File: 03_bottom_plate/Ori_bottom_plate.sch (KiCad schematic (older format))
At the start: 72 parts, among them U1 HOLE, U10 HOLE, U11 HOLE, U12 HOLE, U13 HOLE, U14 HOLE, U15 HOLE, U16 HOLE, U17 HOLE, U18 HOLE, U19 HOLE, U2 HOLE, U20 HOLE, U21 HOLE, U22 HOLE, U23 HOLE, U24 HOLE, U25 HOLE, U26 HOLE, U27 HOLE, U28 HOLE, U29 HOLE, U3 HOLE, U30 HOLE, U31 HOLE, U32 HOLE, U33 HOLE, U34 HOLE, U35 HOLE, U36 HOLE, U37 HOLE, U38 HOLE, U39 HOLE, U4 HOLE, U40 HOLE, U41 HOLE, U42 HOLE, U43 HOLE, U44 HOLE, U45 HOLE, U46 HOLE, U47 HOLE, U48 HOLE, U49 HOLE, U5 HOLE, U53 HOLE, U57 HOLE, U6 HOLE, U61 HOLE, U7 HOLE, U8 HOLE, U9 HOLE

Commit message: 19.05mm spacing; move macro column to right side
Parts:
- removed H1, H2, H3, H4, H5, H6: MountingHole, random-keyboard-parts:Generic-Mounthole, symbol Mechanical:MountingHole
- added D1: DIODE, Keeb_footprints:D_SOD-123_modified, symbol component:DIODE
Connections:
- new net GND: D1.2 (K)
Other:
- moved on the sheet: U49, U53, U57, U61
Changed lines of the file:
@@
 EESchema Schematic File Version 4
-LIBS:Ori_bottom_plate-cache
+LIBS:ori_bottom_plate-cache
 EELAYER 30 0
 EELAYER END
@@
 Comment4 ""
 $EndDescr
-$Comp
-L Mechanical:MountingHole H2
-U 1 1 5DAFB0AC
-P 2600 3300
-F 0 "H2" H 2700 3346 50  0000 L CNN
-F 1 "MountingHole" H 2700 3255 50  0000 L CNN
-F 2 "random-keyboard-parts:Generic-Mounthole" H 2600 3300 50  0001 C CNN
-F 3 "~" H 2600 3300 50  0001 C CNN
-	1    2600 3300
-	1    0    0    -1
-$EndComp
-$Comp
-L Mechanical:MountingHole H1
-U 1 1 5DAFBA19
-P 2600 3100
-F 0 "H1" H 2700 3146 50  0000 L CNN
-F 1 "MountingHole" H 2700 3055 50  0000 L CNN
-F 2 "random-keyboard-parts:Generic-Mounthole" H 2600 3100 50  0001 C CNN
-F 3 "~" H 2600 3100 50  0001 C CNN
-	1    2600 3100
-	1    0    0    -1
-$EndComp
-$Comp
-L Mechanical:MountingHole H3
-U 1 1 5DAFC41A
-P 2600 3500
-F 0 "H3" H 2700 3546 50  0000 L CNN
-F 1 "MountingHole" H 2700 3455 50  0000 L CNN
-F 2 "random-keyboard-parts:Generic-Mounthole" H 2600 3500 50  0001 C CNN
-F 3 "~" H 2600 3500 50  0001 C CNN
-	1    2600 3500
-	1    0    0    -1
-$EndComp
-$Comp
-L Mechanical:MountingHole H4
-U 1 1 5DAFCFC0
-P 2600 3700
-F 0 "H4" H 2700 3746 50  0000 L CNN
-F 1 "MountingHole" H 2700 3655 50  0000 L CNN
-F 2 "random-keyboard-parts:Generic-Mounthole" H 2600 3700 50  0001 C CNN
-F 3 "~" H 2600 3700 50  0001 C CNN
-	1    2600 3700
-	1    0    0    -1
-$EndComp
-$Comp
-L Mechanical:MountingHole H5
-U 1 1 5DAFD908
-P 2600 3900
-F 0 "H5" H 2700 3946 50  0000 L CNN
-F 1 "MountingHole" H 2700 3855 50  0000 L CNN
-F 2 "random-keyboard-parts:Generic-Mounthole" H 2600 3900 50  0001 C CNN
-F 3 "~" H 2600 3900 50  0001 C CNN
-	1    2600 3900
-	1    0    0    -1
-$EndComp
-$Comp
-L Mechanical:MountingHole H6
-U 1 1 5DAFE1B7
-P 2600 4100
-F 0 "H6" H 2700 4146 50  0000 L CNN
-F 1 "MountingHole" H 2700 4055 50  0000 L CNN
-F 2 "random-keyboard-parts:Generic-Mounthole" H 2600 4100 50  0001 C CNN
-F 3 "~" H 2600 4100 50  0001 C CNN
-	1    2600 4100
-	1    0    0    -1
-$EndComp
 Text Notes 2850 4750 0    50   ~ 0
 Screw Holes
@@
 L lets_split-cache:HOLE U49
 U 1 1 5F4BC82B
-P 2250 1550
-F 0 "U49" H 2150 1600 60  0000 L CNN
-F 1 "HOLE" H 2150 1500 60  0000 L CNN
-F 2 "Keeb_footprints:MX100_outline" H 2250 1550 60  0001 C CNN
-F 3 "" H 2250 1550 60  0001 C CNN
-	1    2250 1550
+P 6350 1550
+F 0 "U49" H 6250 1600 60  0000 L CNN
+F 1 "HOLE" H 6250 1500 60  0000 L CNN
+F 2 "Keeb_footprints:MX100_outline" H 6350 1550 60  0001 C CNN
+F 3 "" H 6350 1550 60  0001 C CNN
+	1    6350 1550
 	1    0    0    -1
 $EndComp
@@
 L lets_split-cache:HOLE U53
 U 1 1 5F4BC843
-P 2250 1850
-F 0 "U53" H 2150 1900 60  0000 L CNN
-F 1 "HOLE" H 2150 1800 60  0000 L CNN
-F 2 "Keeb_footprints:MX100_outline" H 2250 1850 60  0001 C CNN
-F 3 "" H 2250 1850 60  0001 C CNN
-	1    2250 1850
+P 6350 1850
+F 0 "U53" H 6250 1900 60  0000 L CNN
+F 1 "HOLE" H 6250 1800 60  0000 L CNN
+F 2 "Keeb_footprints:MX100_outline" H 6350 1850 60  0001 C CNN
+F 3 "" H 6350 1850 60  0001 C CNN
+	1    6350 1850
 	1    0    0    -1
 $EndComp
@@
 L lets_split-cache:HOLE U57
 U 1 1 5F4BC85B
-P 2250 2150
-F 0 "U57" H 2150 2200 60  0000 L CNN
-F 1 "HOLE" H 2150 2100 60  0000 L CNN
-F 2 "Keeb_footprints:MX100_outline" H 2250 2150 60  0001 C CNN
-F 3 "" H 2250 2150 60  0001 C CNN
-	1    2250 2150
+P 6350 2150
+F 0 "U57" H 6250 2200 60  0000 L CNN
+F 1 "HOLE" H 6250 2100 60  0000 L CNN
+F 2 "Keeb_footprints:MX100_outline" H 6350 2150 60  0001 C CNN
+F 3 "" H 6350 2150 60  0001 C CNN
+	1    6350 2150
 	1    0    0    -1
 $EndComp
@@
 L lets_split-cache:HOLE U61
 U 1 1 5F4BC873
-P 2250 2450
-F 0 "U61" H 2150 2500 60  0000 L CNN
-F 1 "HOLE" H 2150 2400 60  0000 L CNN
-F 2 "Keeb_footprints:MX100_outline" H 2250 2450 60  0001 C CNN
-F 3 "" H 2250 2450 60  0001 C CNN
-	1    2250 2450
+P 6350 2450
+F 0 "U61" H 6250 2500 60  0000 L CNN
+F 1 "HOLE" H 6250 2400 60  0000 L CNN
+F 2 "Keeb_footprints:MX100_outline" H 6350 2450 60  0001 C CNN
+F 3 "" H 6350 2450 60  0001 C CNN
+	1    6350 2450
 	1    0    0    -1
 $EndComp
@@
 Wire Notes Line
 	5200 4350 4200 4350
+$Comp
+L component:DIODE D1
+U 1 1 60E9CF4B
+P 6350 3300
+F 0 "D1" H 6350 3492 40  0000 C CNN
+F 1 "DIODE" H 6350 3416 40  0000 C CNN
+F 2 "Keeb_footprints:D_SOD-123_modified" H 6350 3300 50  0001 C CNN
+F 3 "" H 6350 3300 50  0001 C CNN
+	1    6350 3300
+	1    0    0    -1
+$EndComp
+$Comp
+L power:GND #PWR0101
+U 1 1 60E9D8FE
+P 6550 3300
+F 0 "#PWR0101" H 6550 3050 50  0001 C CNN
+F 1 "GND" H 6555 3127 50  0000 C CNN
+F 2 "" H 6550 3300 50  0001 C CNN
+F 3 "" H 6550 3300 50  0001 C CNN
+	1    6550 3300
+	1    0    0    -1
+$EndComp
 $EndSCHEMATC

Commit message: Updated firmware
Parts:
- added H1, H2, H21, H22, H3, H4, H5, H6: MountingHole, random-keyboard-parts:Generic-Mounthole, symbol Mechanical:MountingHole
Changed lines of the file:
@@
 EESchema Schematic File Version 4
-LIBS:ori_bottom_plate-cache
 EELAYER 30 0
 EELAYER END
@@
 	1    0    0    -1
 $EndComp
+$Comp
+L Mechanical:MountingHole H1
+U 1 1 6111B67C
+P 2550 5000
+F 0 "H1" H 2650 5046 50  0000 L CNN
+F 1 "MountingHole" H 2650 4955 50  0000 L CNN
+F 2 "random-keyboard-parts:Generic-Mounthole" H 2550 5000 50  0001 C CNN
+F 3 "~" H 2550 5000 50  0001 C CNN
+	1    2550 5000
+	1    0    0    -1
+$EndComp
+$Comp
+L Mechanical:MountingHole H2
+U 1 1 6111B682
+P 2550 5200
+F 0 "H2" H 2650 5246 50  0000 L CNN
+F 1 "MountingHole" H 2650 5155 50  0000 L CNN
+F 2 "random-keyboard-parts:Generic-Mounthole" H 2550 5200 50  0001 C CNN
+F 3 "~" H 2550 5200 50  0001 C CNN
+	1    2550 5200
+	1    0    0    -1
+$EndComp
+$Comp
+L Mechanical:MountingHole H3
+U 1 1 6111B688
+P 2550 5400
+F 0 "H3" H 2650 5446 50  0000 L CNN
+F 1 "MountingHole" H 2650 5355 50  0000 L CNN
+F 2 "random-keyboard-parts:Generic-Mounthole" H 2550 5400 50  0001 C CNN
+F 3 "~" H 2550 5400 50  0001 C CNN
+	1    2550 5400
+	1    0    0    -1
+$EndComp
+$Comp
+L Mechanical:MountingHole H4
+U 1 1 6111B68E
+P 2550 5600
+F 0 "H4" H 2650 5646 50  0000 L CNN
+F 1 "MountingHole" H 2650 5555 50  0000 L CNN
+F 2 "random-keyboard-parts:Generic-Mounthole" H 2550 5600 50  0001 C CNN
+F 3 "~" H 2550 5600 50  0001 C CNN
+	1    2550 5600
+	1    0    0    -1
+$EndComp
+$Comp
+L Mechanical:MountingHole H5
+U 1 1 6111B694
+P 2550 5800
+F 0 "H5" H 2650 5846 50  0000 L CNN
+F 1 "MountingHole" H 2650 5755 50  0000 L CNN
+F 2 "random-keyboard-parts:Generic-Mounthole" H 2550 5800 50  0001 C CNN
+F 3 "~" H 2550 5800 50  0001 C CNN
+	1    2550 5800
+	1    0    0    -1
+$EndComp
+$Comp
+L Mechanical:MountingHole H6
+U 1 1 6111B69A
+P 2550 6000
+F 0 "H6" H 2650 6046 50  0000 L CNN
+F 1 "MountingHole" H 2650 5955 50  0000 L CNN
+F 2 "random-keyboard-parts:Generic-Mounthole" H 2550 6000 50  0001 C CNN
+F 3 "~" H 2550 6000 50  0001 C CNN
+	1    2550 6000
+	1    0    0    -1
+$EndComp
+$Comp
+L Mechanical:MountingHole H21
+U 1 1 6111ADF9
+P 3650 5050
+F 0 "H21" H 3750 5096 50  0000 L CNN
+F 1 "MountingHole" H 3750 5005 50  0000 L CNN
+F 2 "random-keyboard-parts:Generic-Mounthole" H 3650 5050 50  0001 C CNN
+F 3 "~" H 3650 5050 50  0001 C CNN
+	1    3650 5050
+	1    0    0    -1
+$EndComp
+$Comp
+L Mechanical:MountingHole H22
+U 1 1 6111ADFF
+P 3650 5250
+F 0 "H22" H 3750 5296 50  0000 L CNN
+F 1 "MountingHole" H 3750 5205 50  0000 L CNN
+F 2 "random-keyboard-parts:Generic-Mounthole" H 3650 5250 50  0001 C CNN
+F 3 "~" H 3650 5250 50  0001 C CNN
+	1    3650 5250
+	1    0    0    -1
+$EndComp

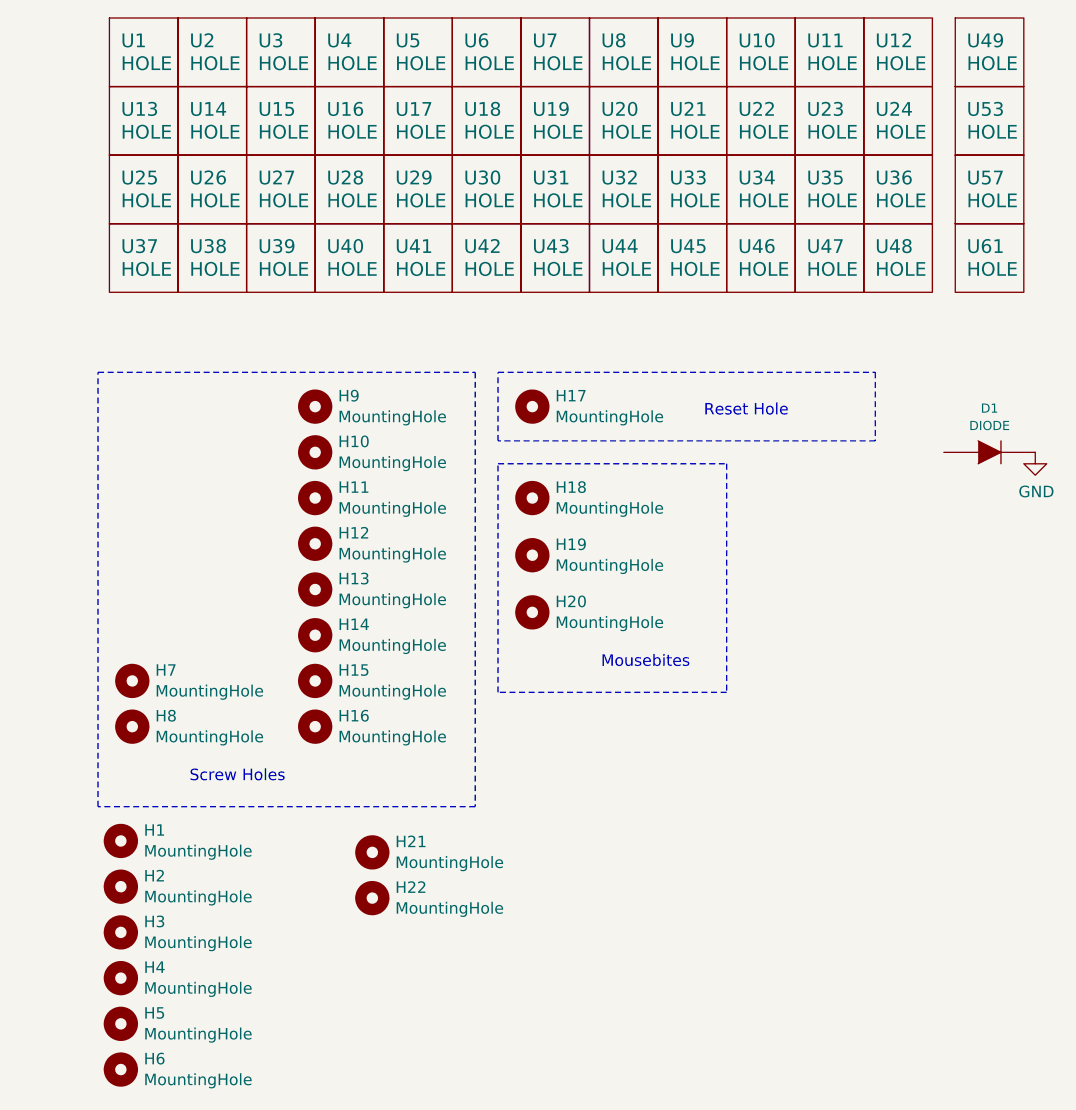
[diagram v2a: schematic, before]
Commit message: added different plate mounts
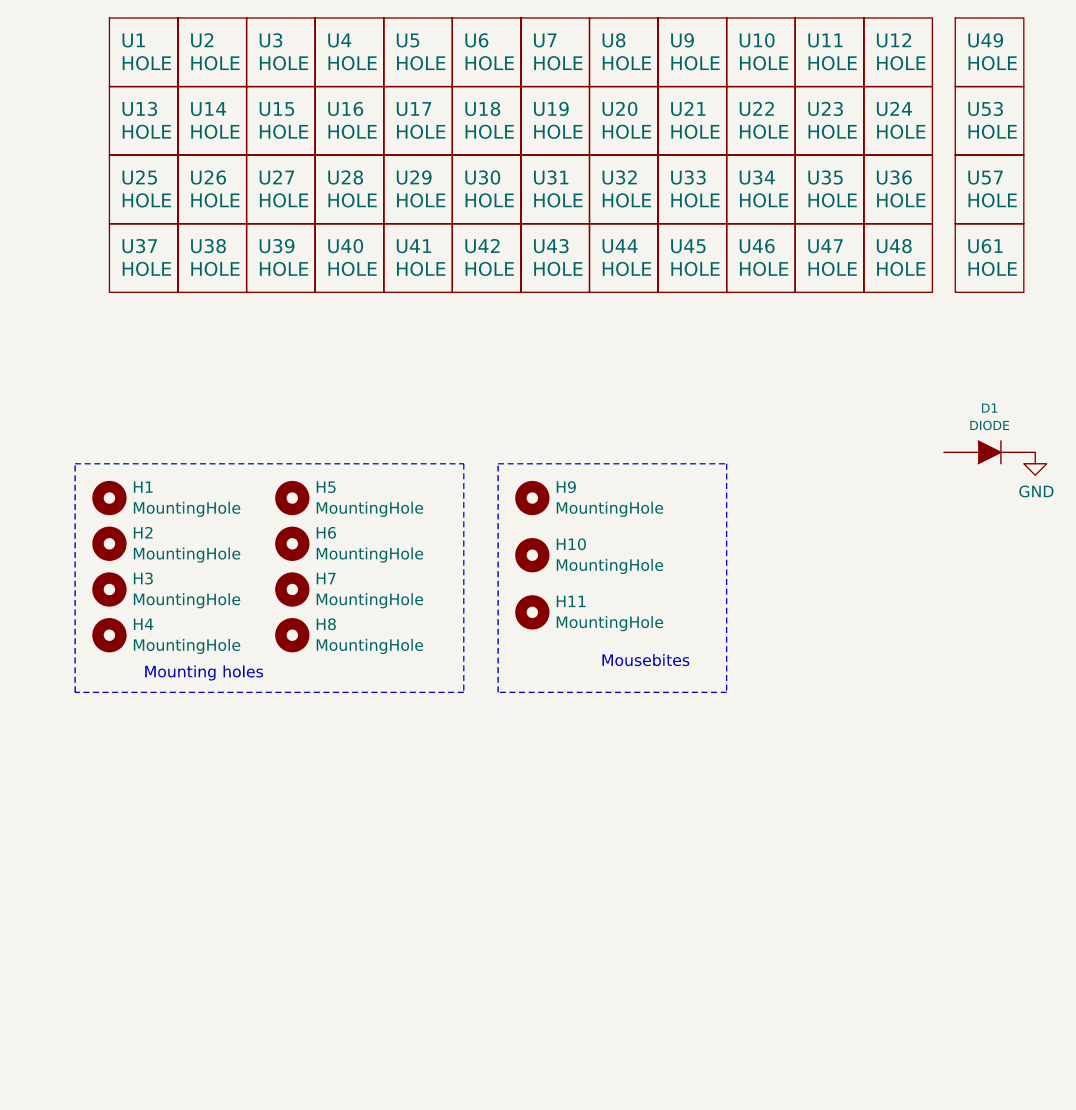
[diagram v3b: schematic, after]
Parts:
- removed H10, H11, H12, H13, H14, H15, H16, H17, H21, H22, H9: MountingHole, random-keyboard-parts:Generic-Mounthole, symbol Mechanical:MountingHole
- renumbered H19 to H10, H20 to H11, H18 to H9
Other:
- note added: "Mounting holes"
- note removed: "Reset Hole"
- note removed: "Screw Holes"
- moved on the sheet: H1, H2, H3, H4, H5, H6, H7, H8

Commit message: modify top plate
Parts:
- added H12: MountingHole, random-keyboard-parts:Generic-Mounthole, symbol Mechanical:MountingHole
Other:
- note added: "Reset hole"
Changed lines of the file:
@@
 Wire Notes Line
 	2350 4350 2350 3350
+$Comp
+L Mechanical:MountingHole H12
+U 1 1 6120175B
+P 2500 4700
+F 0 "H12" H 2600 4746 50  0000 L CNN
+F 1 "MountingHole" H 2600 4655 50  0000 L CNN
+F 2 "random-keyboard-parts:Generic-Mounthole" H 2500 4700 50  0001 C CNN
+F 3 "~" H 2500 4700 50  0001 C CNN
+	1    2500 4700
+	1    0    0    -1
+$EndComp
+Text Notes 2400 4950 0    50   ~ 0
+Reset hole
+Wire Notes Line
+	2350 4550 3300 4550
+Wire Notes Line
+	3300 4550 3300 5000
+Wire Notes Line
+	3300 5000 2350 5000
+Wire Notes Line
+	2350 5000 2350 4550
 $EndSCHEMATC
